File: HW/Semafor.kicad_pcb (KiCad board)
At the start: 2 copper layers, 200 x 200 mm, 88 parts, among them J1 USB_C_Receptacle_USB2.0, J2 USB_plug, M1 Motor_DC, Q1 Q_NMOS_GSD, Q2 Q_NMOS_GSD, Q3 Q_NMOS_GSD, Q4 Q_NMOS_GSD, SW6 SW_SPDT, U1 ESP32-C3, U2 CN3058E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

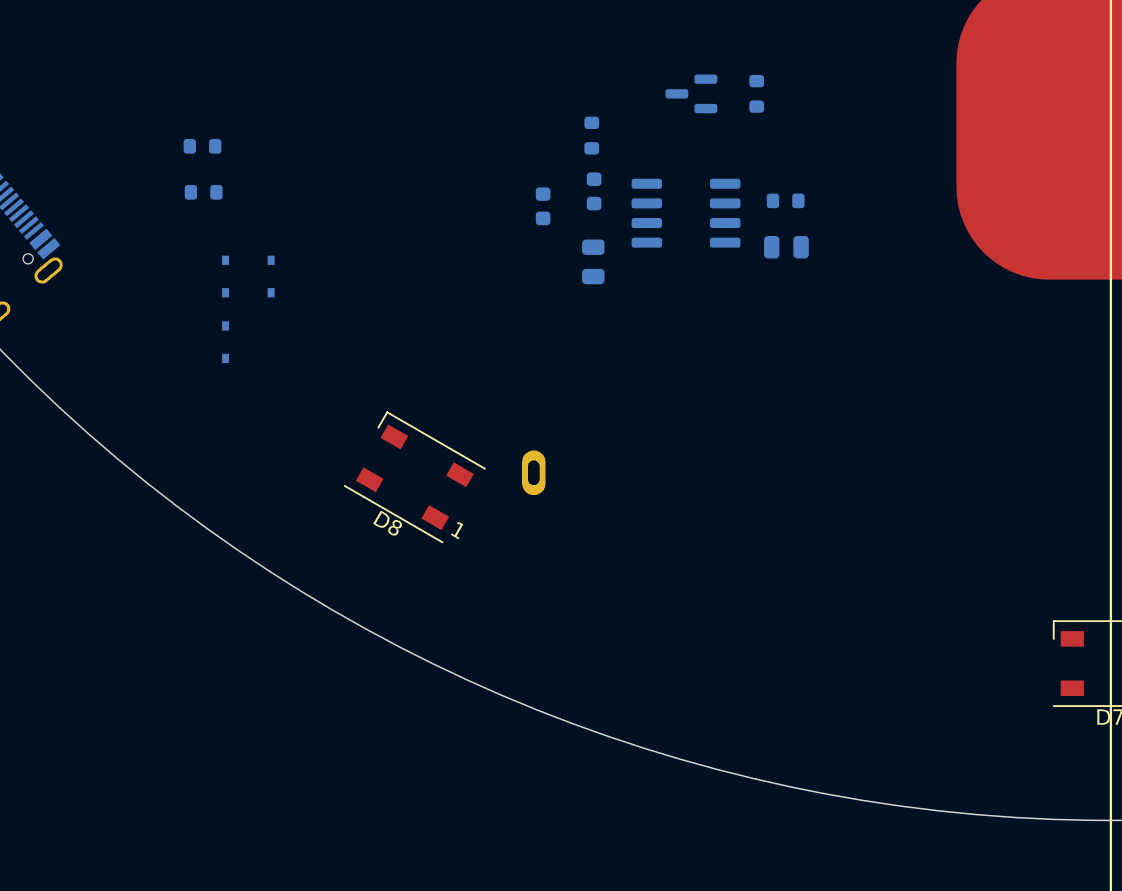
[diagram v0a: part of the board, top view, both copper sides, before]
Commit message: add some datasheets, add diodes to USBs
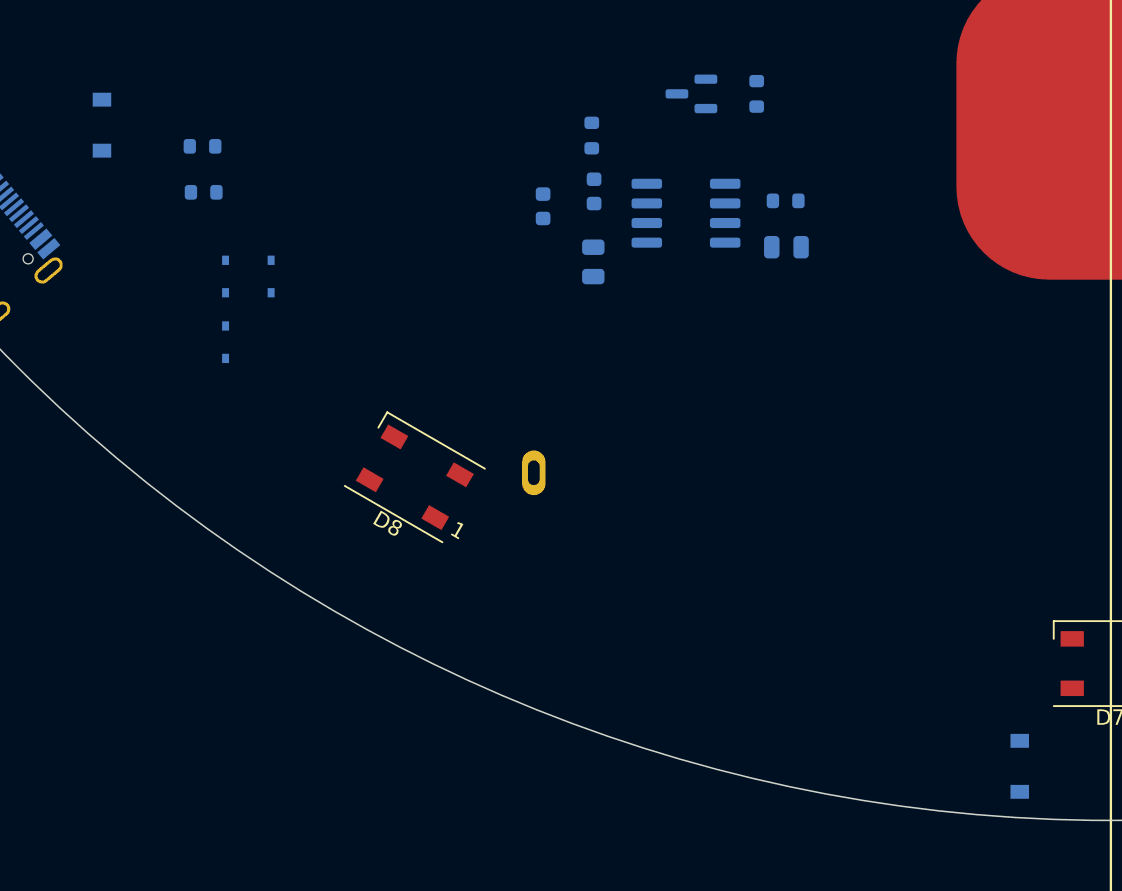
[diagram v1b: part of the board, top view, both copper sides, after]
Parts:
- added D23: D_Schottky, Diode_SMD:D_SOD-123, B.Cu at (-105.9, -3.50)
- added D24: D_Schottky, Diode_SMD:D_SOD-123, B.Cu at (-165.3, -45.0)
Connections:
- J1 pad A4: +5V -> Net-(J1-PadA4)
- J1 pad A9: +5V -> Net-(J1-PadA4)
- J1 pad B4: +5V -> Net-(J1-PadA4)
- J1 pad B9: +5V -> Net-(J1-PadA4)
- J2 pad 1: unconnected-(J2-Pad1) -> Net-(J2-Pad1)
- Q2 pad 2: Net-(BT1-Pad1) -> +3V3

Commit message: routing PCB - LEDs
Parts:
- removed Q2: Q_NMOS_GSD, Package_TO_SOT_SMD:SOT-23
- removed R1: 1M, Resistor_SMD:R_0603_1608Metric
- added D25: SD05_SOD323, Diode_SMD:D_SOD-323, B.Cu at (-88.6, -4.67)
- R10: value 22k -> 13k
- R2, R3: footprint Resistor_SMD:R_0603_1608Metric -> Resistor_SMD:R_0402_1005Metric
- R9: value 10k -> 39k
- moved D22 229.0 mm to (44.9, -36.8)
- moved M1 229.0 mm to (66.5, -47.9)
- moved R15 229.0 mm to (49.8, -37.2)
- moved BZ1 229.0 mm to (31.3, -51.6)
- moved D21 229.0 mm to (31.7, -35.9)
- moved Q4 229.0 mm to (37.0, -35.4)
- moved R14 229.0 mm to (41.5, -33.9)
- moved C25 229.0 mm to (30.8, -33.0)
- moved Q3 229.0 mm to (56.9, -41.5)
- moved C12 203.4 mm to (-143.0, -174.9), turned to -150 degrees
- moved C19 197.8 mm to (-174.7, -142.6), turned to -120 degrees
- moved C23 191.0 mm to (-99.3, -186.2), turned to 180 degrees
- moved C17 184.4 mm to (-185.9, -100.5), turned to -90 degrees
- moved C16 171.9 mm to (-57.5, -174.8), turned to 150 degrees
- moved C18 155.3 mm to (-174.9, -57.9), turned to -60 degrees
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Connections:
- C10 pad 1: Net-(C10-Pad1) -> +3V3
- D11 pad 4: Net-(D11-Pad4) -> Net-(D10-Pad2)
- D12 pad 4: Net-(D10-Pad2) -> Net-(D11-Pad2)
- D2 pad 4: Net-(D11-Pad2) -> Net-(D1-Pad2)
- D3 pad 4: Net-(D1-Pad2) -> Net-(D2-Pad2)
- D4 pad 4: Net-(D2-Pad2) -> Net-(D3-Pad2)
- D5 pad 4: Net-(D3-Pad2) -> Net-(D4-Pad2)
- D6 pad 4: Net-(D4-Pad2) -> Net-(D5-Pad2)
- D7 pad 2: Net-(D10-Pad4) -> Net-(D7-Pad2)
- D8 pad 4: Net-(D5-Pad2) -> Net-(D7-Pad2)
- D9 pad 2: Net-(D11-Pad4) -> Net-(D10-Pad4)
- U2 pad 5: Net-(C10-Pad1) -> +3V3
- U2 pad 8: Net-(C10-Pad1) -> +3V3
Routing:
- net GND: track 0.00 -> 839.2 mm
- net PWR_LED: track 0.00 -> 583.8 mm
- net Net-(D10-Pad2): track 0.00 -> 45.4 mm
- net Net-(D7-Pad2): track 0.00 -> 45.4 mm
- net Net-(D1-Pad2): track 0.00 -> 45.4 mm
- net Net-(D4-Pad2): track 0.00 -> 45.4 mm
- net Net-(D6-Pad2): track 0.00 -> 44.5 mm
- net Net-(D10-Pad4): track 0.00 -> 44.5 mm
- net Net-(D3-Pad2): track 0.00 -> 44.5 mm
- net Net-(D5-Pad2): track 0.00 -> 43.1 mm
- net Net-(D2-Pad2): track 0.00 -> 43.1 mm
- net Net-(D11-Pad2): track 0.00 -> 43.1 mm
- net Net-(D8-Pad2): track 0.00 -> 43.1 mm

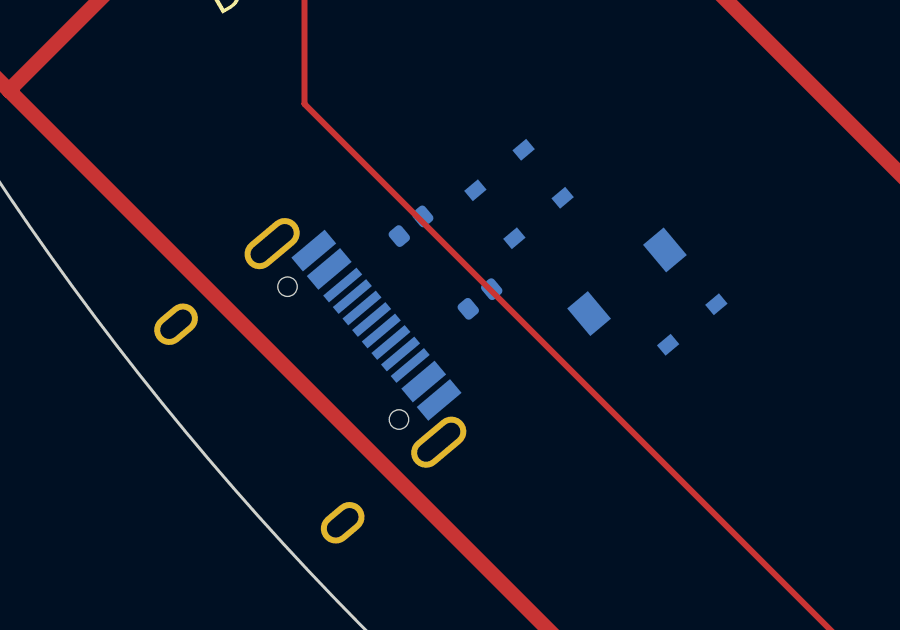
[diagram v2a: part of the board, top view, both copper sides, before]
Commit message: add fill of description field
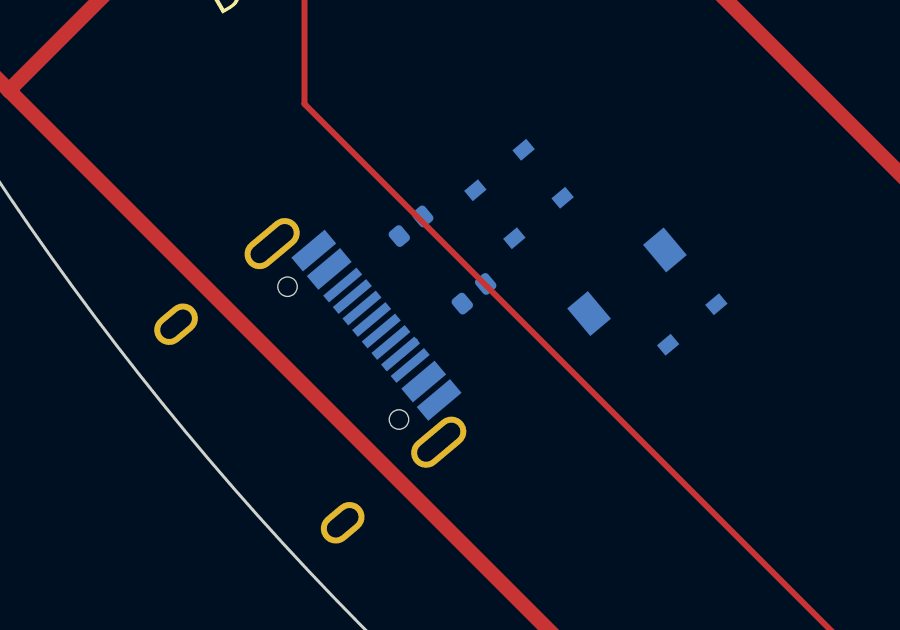
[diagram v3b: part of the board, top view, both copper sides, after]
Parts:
- moved R2 0.27 mm to (-167.3, -40.8)
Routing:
- net Net-(J1-PadA5): track 0.00 -> 0.66 mm
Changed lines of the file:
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@@
   )
   (footprint "Resistor_SMD:R_0402_1005Metric" (layer "B.Cu")
-    (at -167.15 -40.575 40)
+    (at -167.35 -40.75 40)
     (descr "Resistor SMD 0402 (1005 Metric), square (rectangular) end terminal, IPC_7351 nominal, (Body size source: IPC-SM-782 page 72, https://www.pcb-3d.com/wordpress/wp-content/uploads/ipc-sm-782a_amendment_1_and_2.pdf), generated with kicad-footprint-generator")
     (tags "resistor")
@@
   (segment (start -19.497072 -143.828238) (end -17.55 -141.881166) (width 0.2) (layer "F.Cu") (net 25))
   (segment (start -11.65 -106.75) (end -11.65 -102.6) (width 0.2) (layer "F.Cu") (net 25))
+  (segment (start -169.73748 -38.74252) (end -169.31 -39.17) (width 0.2) (layer "B.Cu") (net 37))
+  (segment (start -169.797866 -38.74252) (end -169.73748 -38.74252) (width 0.2) (layer "B.Cu") (net 37))
   (segment (start -56.8125 -174.4625) (end -55.779942 -173.429942) (width 0.5) (layer "F.Cu") (net 43))
   (segment (start -24.9125 -142.17883) (end -24.9125 -142.1625) (width 0.5) (layer "F.Cu") (net 43))

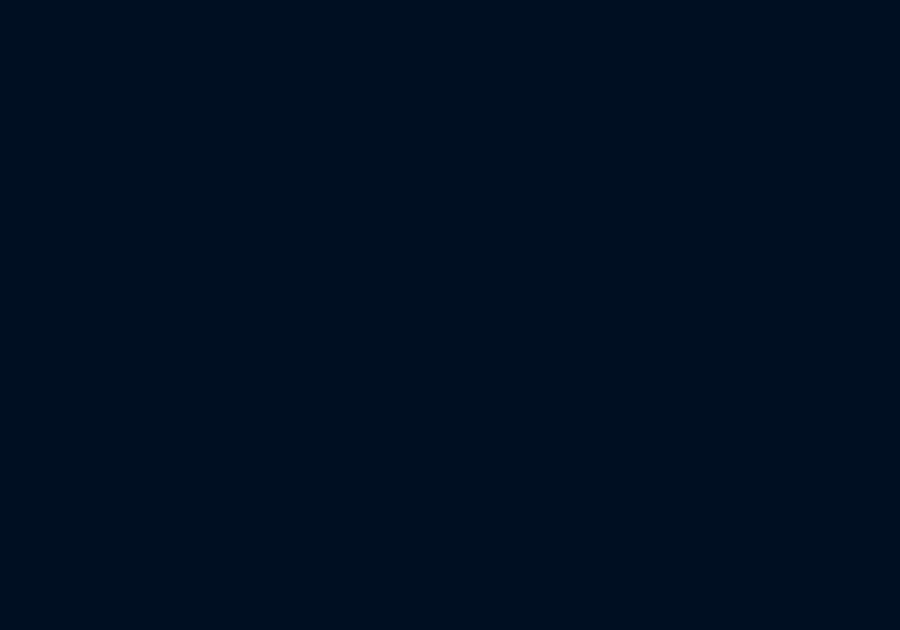
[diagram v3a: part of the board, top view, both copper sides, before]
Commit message: add voltage reference
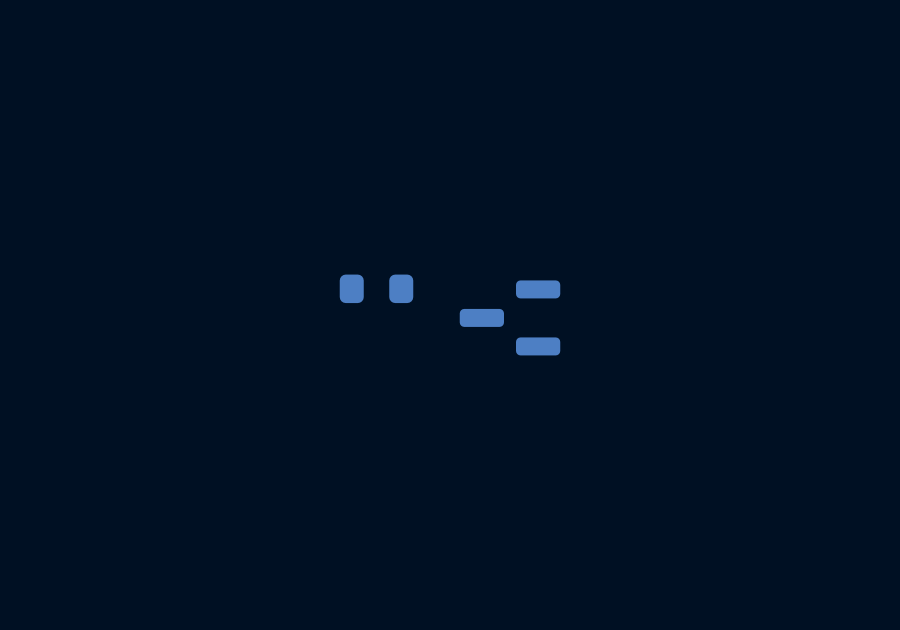
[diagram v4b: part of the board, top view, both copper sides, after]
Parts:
- added R1: 10k, Resistor_SMD:R_0603_1608Metric, B.Cu at (-223.2, -121.9)
- added U6: CJ431, Package_TO_SOT_SMD:SOT-23, B.Cu at (-218.8, -120.9)
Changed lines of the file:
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@@
   (net 74 "Net-(R21-Pad2)")
   (net 75 "Net-(R22-Pad1)")
+  (net 76 "U_BAT_ADC")
   (footprint "Library:Cap_btn_2x2" (layer "F.Cu")
     (at -93.7 -62.3)
@@
     )
   )
+  (footprint "Resistor_SMD:R_0603_1608Metric" (layer "B.Cu")
+    (at -223.229524 -121.9 180)
+    (descr "Resistor SMD 0603 (1608 Metric), square (rectangular) end terminal, IPC_7351 nominal, (Body size source: IPC-SM-782 page 72, https://www.pcb-3d.com/wordpress/wp-content/uploads/ipc-sm-782a_amendment_1_and_2.pdf), generated with kicad-footprint-generator")
+    (tags "resistor")
+    (property "Sheetfile" "Semafor.kicad_sch")
+    (property "Sheetname" "")
+    (attr smd)
+    (fp_text reference "R1" (at 0 1.43) (layer "B.SilkS")
+      (effects (font (size 1 1) (thickness 0.15)) (justify mirror))
+    )
+    (fp_text value "10k" (at 0 -1.43) (layer "B.Fab")
+      (effects (font (size 1 1) (thickness 0.15)) (justify mirror))
+    )
+    (fp_text user "${REFERENCE}" (at 0 0) (layer "B.Fab")
+      (effects (font (size 0.4 0.4) (thickness 0.06)) (justify mirror))
+    )
+    (fp_line (start -0.237258 0.5225) (end 0.237258 0.5225) (layer "B.SilkS") (width 0.12))
+    (fp_line (start -0.237258 -0.5225) (end 0.237258 -0.5225) (layer "B.SilkS") (width 0.12))
+    (fp_line (start 1.48 -0.73) (end -1.48 -0.73) (layer "B.CrtYd") (width 0.05))
+    (fp_line (start 1.48 0.73) (end 1.48 -0.73) (layer "B.CrtYd") (width 0.05))
+    (fp_line (start -1.48 -0.73) (end -1.48 0.73) (layer "B.CrtYd") (width 0.05))
+    (fp_line (start -1.48 0.73) (end 1.48 0.73) (layer "B.CrtYd") (width 0.05))
+    (fp_line (start -0.8 -0.4125) (end -0.8 0.4125) (layer "B.Fab") (width 0.1))
+    (fp_line (start -0.8 0.4125) (end 0.8 0.4125) (layer "B.Fab") (width 0.1))
+    (fp_line (start 0.8 0.4125) (end 0.8 -0.4125) (layer "B.Fab") (width 0.1))
+    (fp_line (start 0.8 -0.4125) (end -0.8 -0.4125) (layer "B.Fab") (width 0.1))
+    (pad "1" smd roundrect (at -0.825 0 180) (size 0.8 0.95) (layers "B.Cu" "B.Paste" "B.Mask") (roundrect_rratio 0.25)
+      (net 27 "+3V3") (pintype "passive"))
+    (pad "2" smd roundrect (at 0.825 0 180) (size 0.8 0.95) (layers "B.Cu" "B.Paste" "B.Mask") (roundrect_rratio 0.25)
+      (net 76 "U_BAT_ADC") (pintype "passive"))
+    (model "${KICAD6_3DMODEL_DIR}/Resistor_SMD.3dshapes/R_0603_1608Metric.wrl"
+      (offset (xyz 0 0 0))
+      (scale (xyz 1 1 1))
+      (rotate (xyz 0 0 0))
+    )
+  )
   (footprint "Capacitor_SMD:C_0805_2012Metric" (layer "B.Cu")
     (at -172.25 -124.05 90)
@@
       (offset (xyz 0 0 0))
       (scale (xyz 1 1 1))
+      (rotate (xyz 0 0 0))
+    )
+  )
+  (footprint "Package_TO_SOT_SMD:SOT-23" (layer "B.Cu")
+    (at -218.779524 -120.93 180)
+    (descr "SOT, 3 Pin (https://www.jedec.org/system/files/docs/to-236h.pdf variant AB), generated with kicad-footprint-generator ipc_gullwing_generator.py")
+    (tags "SOT TO_SOT_SMD")
+    (property "LCSC" "C3113")
+    (property "Sheetfile" "Semafor.kicad_sch")
+    (property "Sheetname" "")
+    (attr smd)
+    (fp_text reference "U6" (at 0 2.4) (layer "B.SilkS")
+      (effects (font (size 1 1) (thickness 0.15)) (justify mirror))
+    )
+    (fp_text value "CJ431" (at 0 -2.4) (layer "B.Fab")
+      (effects (font (size 1 1) (thickness 0.15)) (justify mirror))
+    )
+    (fp_text user "${REFERENCE}" (at 0 0) (layer "B.Fab")
+      (effects (font (size 0.32 0.32) (thickness 0.05)) (justify mirror))
+    )
+    (fp_line (start 0 1.56) (end 0.65 1.56) (layer "B.SilkS") (width 0.12))
+    (fp_line (start 0 -1.56) (end -0.65 -1.56) (layer "B.SilkS") (width 0.12))
+    (fp_line (start 0 1.56) (end -1.675 1.56) (layer "B.SilkS") (width 0.12))
+    (fp_line (start 0 -1.56) (end 0.65 -1.56) (layer "B.SilkS") (width 0.12))
+    (fp_line (start -1.92 -1.7) (end 1.92 -1.7) (layer "B.CrtYd") (width 0.05))
+    (fp_line (start 1.92 1.7) (end -1.92 1.7) (layer "B.CrtYd") (width 0.05))
+    (fp_line (start 1.92 -1.7) (end 1.92 1.7) (layer "B.CrtYd") (width 0.05))
+    (fp_line (start -1.92 1.7) (end -1.92 -1.7) (layer "B.CrtYd") (width 0.05))
+    (fp_line (start -0.325 1.45) (end 0.65 1.45) (layer "B.Fab") (width 0.1))
+    (fp_line (start -0.65 1.125) (end -0.325 1.45) (layer "B.Fab") (width 0.1))
+    (fp_line (start 0.65 -1.45) (end -0.65 -1.45) (layer "B.Fab") (width 0.1))
+    (fp_line (start 0.65 1.45) (end 0.65 -1.45) (layer "B.Fab") (width 0.1))
+    (fp_line (start -0.65 -1.45) (end -0.65 1.125) (layer "B.Fab") (width 0.1))
+    (pad "1" smd roundrect (at -0.9375 0.95 180) (size 1.475 0.6) (layers "B.Cu" "B.Paste" "B.Mask") (roundrect_rratio 0.25)
+      (net 76 "U_BAT_ADC") (pinfunction "REF") (pintype "passive"))
+    (pad "2" smd roundrect (at -0.9375 -0.95 180) (size 1.475 0.6) (layers "B.Cu" "B.Paste" "B.Mask") (roundrect_rratio 0.25)
+      (net 27 "+3V3") (pinfunction "K") (pintype "passive"))
+    (pad "3" smd roundrect (at 0.9375 0 180) (size 1.475 0.6) (layers "B.Cu" "B.Paste" "B.Mask") (roundrect_rratio 0.25)
+      (net 1 "GND") (pinfunction "A") (pintype "passive"))
+    (model "${KICAD6_3DMODEL_DIR}/Package_TO_SOT_SMD.3dshapes/SOT-23.wrl"
+      (offset (xyz 0 0 0))
+      (scale (xyz 1 1 1))
